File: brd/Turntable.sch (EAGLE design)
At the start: 115 parts, among them CON1 Pannel, CON2 CAN, CON3 Turntable, CON4 STEPPER_CON, CON5 STEPPER_CON, CON8 SPK, IC1 7805, IC2 LM393N, J1 MiniStp2, J10 MiniStp1, Q1 BS170, SW1 EC12E_SW, U2 LED NANO, X1 AK500/2+M, X2 AK500/2+M, X3 MAB 5SH Conrad: 738247 - VQ, X4 AK500/2+M, X5 Reichelt MEBP 8-8S

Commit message: Correchted spelling
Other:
- note added: "Bei Drehscheiben mit nur 3 oder 4 Schleifringen kann das Licht und die Warnlampe über eine Leitung mit der Schienenspannung betrieben werden. Zur Trennung werden die Optokoppler verwendet. Dabei nutzt die Schaltung die Tatsache, dass die Schienenspannung Wechselspannung ist."
- note added: "J10 für Tests mit winzigen Steppern für Signale oder Weichen"
- note added: "Optional kann auch ein WS2812 LED Bus zur Bühne verwendet werden. Dann entfallen die Optokoppler und DIR_LIGHT wird verbunden."
- note removed: "Bei Drehscheiben mit nur 3 oder 4 Schleifringen kann das Licht und die Warnlampe über eine Leitung mit der Schinenspannung betrieben werden. Zur Trennung werden die Optokopler verwendet. Dabei nutzt die Schaltung die Tatsache, dass die Schinenspannung Wechselspannung ist."
- note removed: "J10 für Tests mit minzigen Steppern für Signale oder Weichen"
- note removed: "Optional kann auch ein WS2812 LED Bus zur Bühne verwendet werden. Dann entfallen die Optopopler und DIR_LIGHT wird verbunden."
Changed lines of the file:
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@@
 <wire x1="288.29" y1="147.32" x2="314.96" y2="147.32" width="0.1524" layer="95" style="shortdash"/>
 <text x="294.64" y="243.84" size="1.778" layer="150">Bei Drehscheiben mit nur 3 oder 4 Schleifringen kann das Licht und die
-Warnlampe über eine Leitung mit der Schinenspannung betrieben werden.
-Zur Trennung werden die Optokopler verwendet. Dabei nutzt die Schaltung
-die Tatsache, dass die Schinenspannung Wechselspannung ist.</text>
+Warnlampe über eine Leitung mit der Schienenspannung betrieben werden.
+Zur Trennung werden die Optokoppler verwendet. Dabei nutzt die Schaltung
+die Tatsache, dass die Schienenspannung Wechselspannung ist.</text>
 <wire x1="364.49" y1="213.36" x2="367.03" y2="213.36" width="0.1524" layer="150"/>
 <wire x1="367.03" y1="213.36" x2="365.76" y2="210.82" width="0.1524" layer="150"/>
@@
 <text x="269.24" y="198.12" size="1.778" layer="150" rot="R180">Optional kann auch ein WS2812 LED
 Bus zur Bühne verwendet werden.
-Dann entfallen die Optopopler und
+Dann entfallen die Optokoppler und
 DIR_LIGHT wird verbunden.</text>
 <text x="377.19" y="179.07" size="1.778" layer="150" rot="R90">Diese Schaltung wird auf
@@
 wenn von DCC
 versorgt.</text>
-<text x="144.78" y="124.46" size="1.524" layer="97" align="top-left">Anzeige: Scheibe
+<text x="147.32" y="124.46" size="1.524" layer="97" align="top-left">Anzeige: Scheibe
 dreht sich
 </text>
@@
 28BYJ-48</text>
 <text x="359.41" y="46.99" size="1.778" layer="150">J10 für Tests mit
-minzigen Steppern
+winzigen Steppern
 für Signale oder
 Weichen</text>

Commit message: Update Turntable.sch
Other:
- note added: "Der TMC2100 ist viel leiser Achtung: - Strom vor Anschluss des Steppers einstellen - Einbaurichtung beachten. Beim TMC2100 ist das Poti oben"
- note removed: "Der TDS2100 ist viel leiser Achtung: - Strom vor Anschluss des Steppers einstellen - Einbaurichtung beachten. Beim TDS2100 ist das Poti oben"
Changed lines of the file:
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@@
 für Signale oder
 Weichen</text>
-<text x="295.91" y="29.21" size="1.778" layer="150">Der TDS2100 ist viel leiser
+<text x="295.91" y="29.21" size="1.778" layer="150">Der TMC2100 ist viel leiser
 Achtung:
 - Strom vor Anschluss des Steppers einstellen
 - Einbaurichtung beachten.
-  Beim TDS2100 ist das Poti oben</text>
+  Beim TMC2100 ist das Poti oben</text>
 <wire x1="364.8075" y1="218.44" x2="365.76" y2="218.44" width="0.1524" layer="150"/>
 <wire x1="365.76" y1="218.44" x2="366.7125" y2="218.44" width="0.1524" layer="150"/>

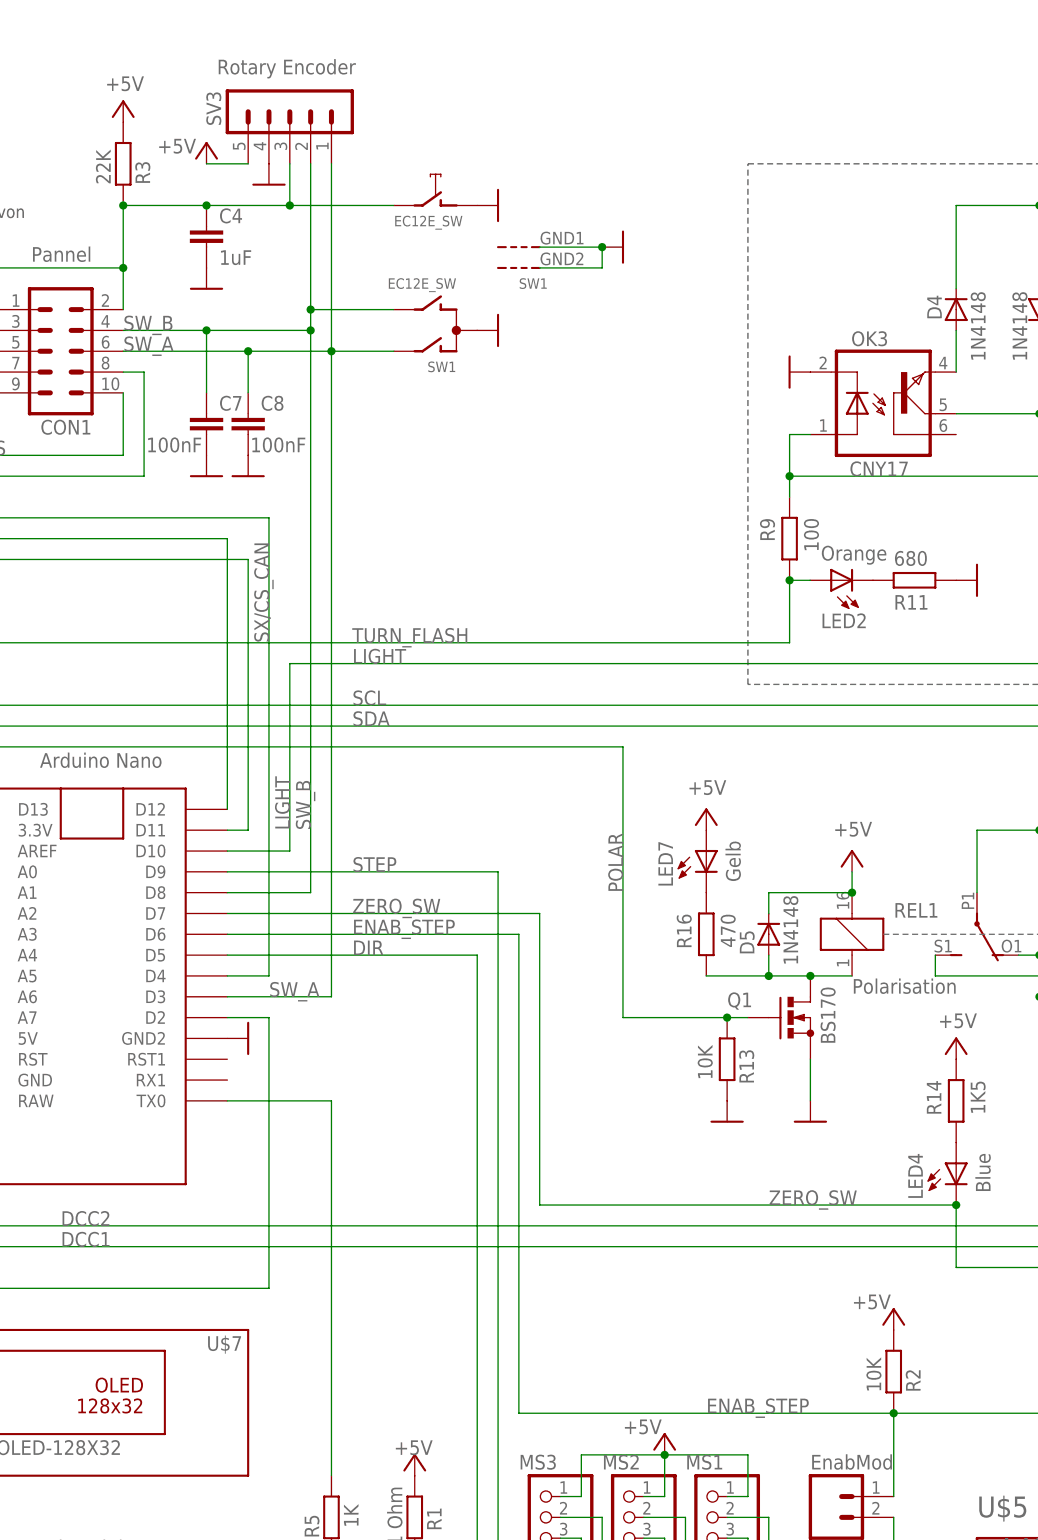
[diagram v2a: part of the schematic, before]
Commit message: Corrected Potary Encoder Pins
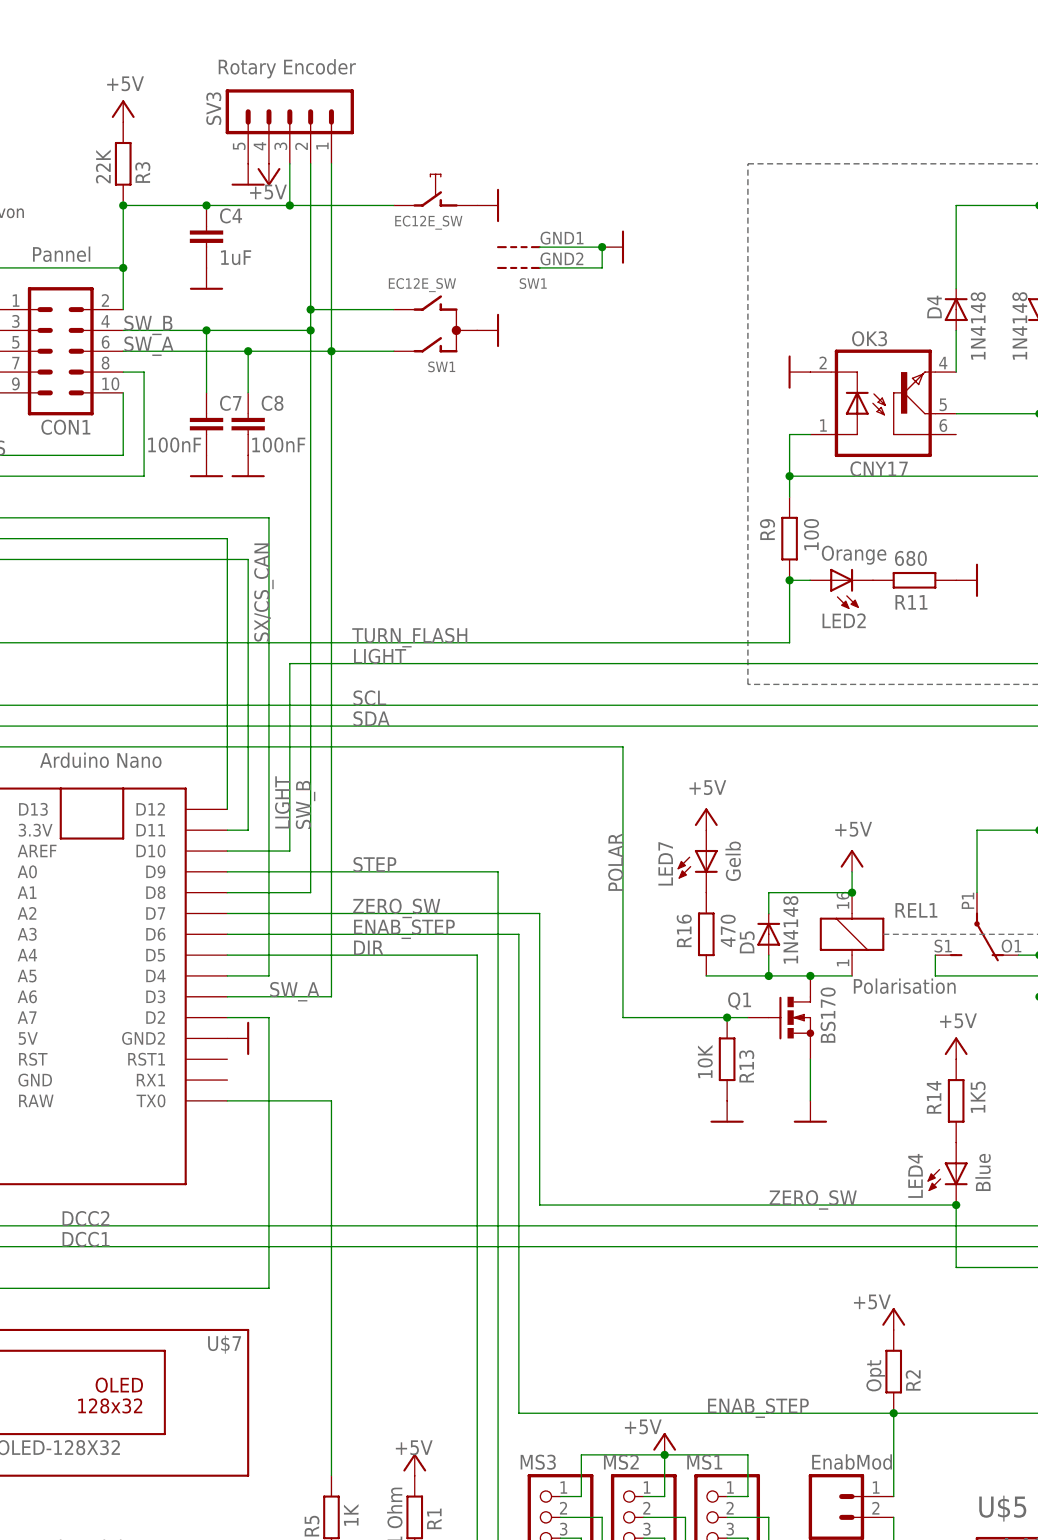
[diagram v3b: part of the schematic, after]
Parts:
- R2: value 10K -> Opt
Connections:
- net +5V: now also SV3.4; no longer SV3.5
- net GND: now also SV3.5; no longer SV3.4
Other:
- note added: "Mit 10K Bestücken damit der Stepper nicht während des Prog. heiß wird"
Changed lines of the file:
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@@
 <part name="JP1" library="adafruit" deviceset="PINHD-1X3" device="CB" value="MS1"/>
 <part name="JP4" library="SparkFun-Connectors" deviceset="M02" device="PTH" value="EnabMod"/>
-<part name="R2" library="rcl" deviceset="R-EU_" device="0204/7" value="10K"/>
+<part name="R2" library="rcl" deviceset="R-EU_" device="0204/7" value="Opt"/>
 <part name="P+3" library="supply1" library_urn="urn:adsk.eagle:library:371" deviceset="+5V" device=""/>
 <part name="P+6" library="supply1" library_urn="urn:adsk.eagle:library:371" deviceset="+5V" device=""/>
@@
 <part name="P+25" library="supply1" library_urn="urn:adsk.eagle:library:371" deviceset="+5V" device=""/>
 <part name="SV3" library="con-lstb" deviceset="MA05-1" device="SMALL_PAD" value="Rotary Encoder"/>
+<part name="P+26" library="supply1" library_urn="urn:adsk.eagle:library:371" deviceset="+5V" device=""/>
 <part name="GND46" library="supply1" deviceset="GND" device=""/>
-<part name="P+26" library="supply1" library_urn="urn:adsk.eagle:library:371" deviceset="+5V" device=""/>
 </parts>
 <sheets>
@@
 <wire x1="372.745" y1="224.79" x2="375.92" y2="224.79" width="0.1524" layer="150"/>
 <text x="371.475" y="217.805" size="1.4224" layer="150" rot="R90">47uF 25V</text>
+<text x="295.91" y="90.17" size="1.778" layer="150">Mit 10K Bestücken
+damit der Stepper nicht
+während des Prog. heiß wird</text>
 </plain>
 <instances>
@@
 <attribute name="NAME" x="207.518" y="250.19" size="1.778" layer="95" rot="MR270"/>
 </instance>
-<instance part="GND46" gate="1" x="213.36" y="238.76" smashed="yes" rot="MR0"/>
-<instance part="P+26" gate="1" x="205.74" y="243.84" smashed="yes" rot="MR0">
-<attribute name="VALUE" x="204.47" y="242.57" size="1.778" layer="96" rot="MR0"/>
-</instance>
+<instance part="P+26" gate="1" x="213.36" y="238.76" smashed="yes" rot="MR180">
+<attribute name="VALUE" x="210.82" y="238.76" size="1.778" layer="96" rot="MR180"/>
+</instance>
+<instance part="GND46" gate="1" x="210.82" y="238.76" smashed="yes" rot="MR0"/>
 </instances>
 <busses>
@@
 </segment>
 <segment>
-<pinref part="SV3" gate="G$1" pin="4"/>
+<pinref part="SV3" gate="G$1" pin="5"/>
 <pinref part="GND46" gate="1" pin="GND"/>
 </segment>
@@
 </segment>
 <segment>
+<pinref part="SV3" gate="G$1" pin="4"/>
 <pinref part="P+26" gate="1" pin="+5V"/>
-<pinref part="SV3" gate="G$1" pin="5"/>
-<wire x1="205.74" y1="241.3" x2="210.82" y2="241.3" width="0.1524" layer="91"/>
 </segment>
 </net>

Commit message: Final Version 1.0
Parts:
- added JP20, JP21: Mode, adafruit:PINHD-1X3CB
- JP4, JP8: value EnabMod -> Enab; device SparkFun-Connectors:M02PTH -> adafruit:PINHD-1X3CB
- R19: value 10K -> Opt
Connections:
- new net N$32: JP21.3, U$1.!SLEEP
- new net N$33: JP20.3, U$5.!SLEEP
- net +5V: now also JP4.1, JP8.1
- net ENAB_STEP: now also JP20.1, JP4.3; no longer JP4.1
- net N$30: now also JP20.2; no longer U$5.!SLEEP
- net N$46: now also JP21.2; no longer U$1.!SLEEP
- net SX/CS_CAN: now also JP21.1, JP8.3; no longer JP8.1
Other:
- note added: "A4988, TMC2100 oder TMC2208"
- note added: "TCM2208: NC PDN_UART CLK"
- moved on the sheet: C6, JP1, JP2, JP3, JP5, JP6, JP7, LED1, OK2, R1, R17, R18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
